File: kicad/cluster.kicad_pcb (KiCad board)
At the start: 2 copper layers, 24.5 x 33.5 mm, 16 parts, among them J1 Conn_01x07, Q1 PT908-7B-F, Q2 PT908-7B-F, Q3 PT908-7B-F, Q4 PT908-7B-F, Q5 PT908-7B-F

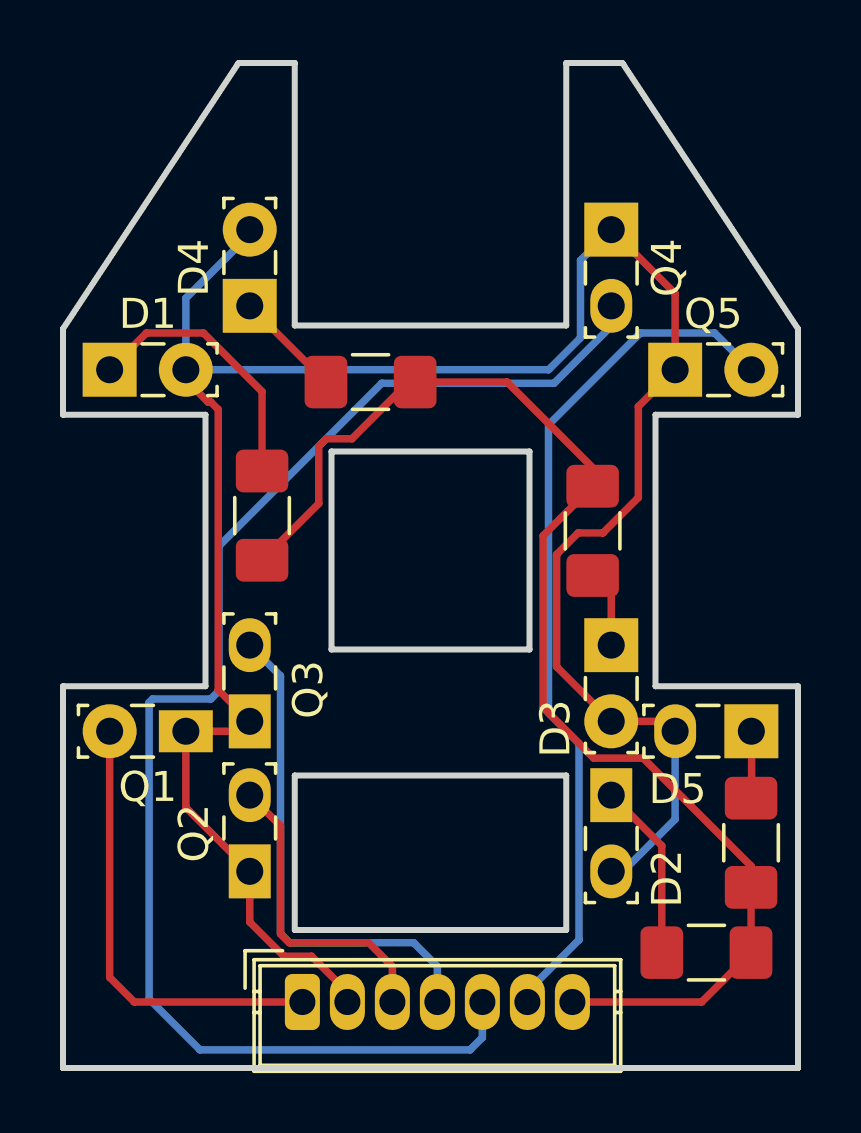
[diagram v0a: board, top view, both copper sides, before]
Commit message: Update the names for the LEDs and PTs on the finger cluster pcb
Q -> PT
D -> IR
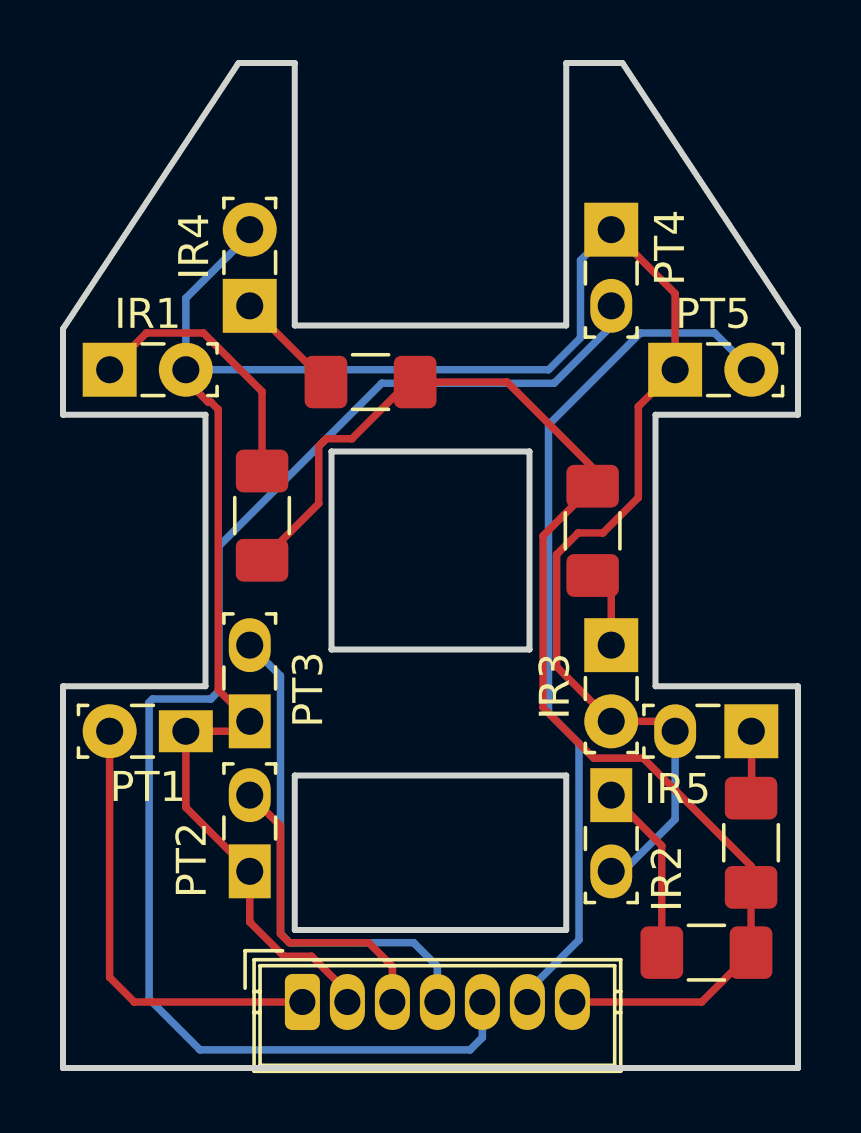
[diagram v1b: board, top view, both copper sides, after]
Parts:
- renumbered D1 to IR1, D2 to IR2, D3 to IR3, D4 to IR4, D5 to IR5, Q1 to PT1, Q2 to PT2, Q3 to PT3, Q4 to PT4, Q5 to PT5

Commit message: Add a nub indicating the lens on the IR and PT footprints
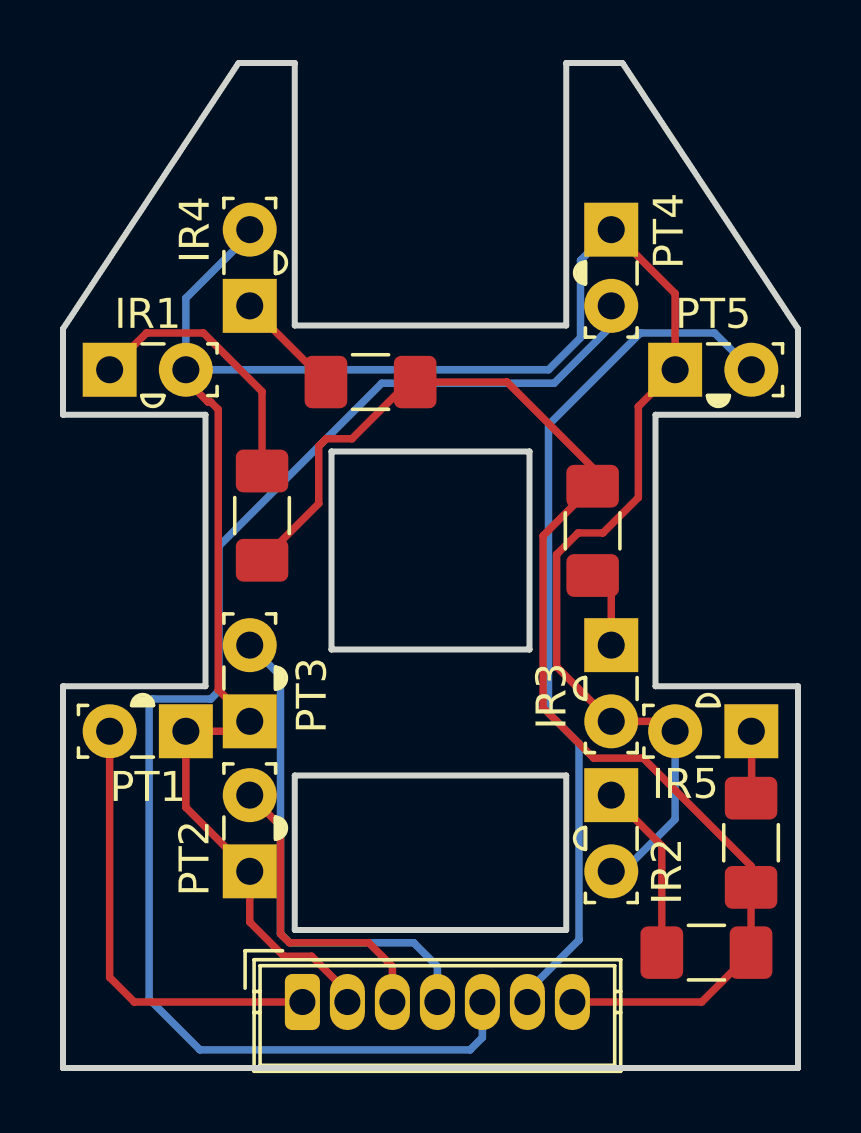
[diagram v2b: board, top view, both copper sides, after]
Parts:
- IR1, IR2, IR3, IR4, IR5: footprint LED_THT:LED_SideEmitter_Rectangular_W4.5mm_H1.6mm -> lalboard:IR908-7C-F
- PT1, PT2, PT3, PT4, PT5: footprint LED_THT:LED_SideEmitter_Rectangular_W4.5mm_H1.6mm -> lalboard:PT908-7C-F
